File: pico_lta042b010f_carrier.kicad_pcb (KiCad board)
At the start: 2 copper layers, 100 x 52 mm, 31 parts, among them J1 LTA042B010F_FFC_36P_0.5mm, J2 USB-C 5V INPUT, J3 CCFL_INVERTER_13V8, U1 RaspberryPi_Pico_2W, U3 MC34063AD

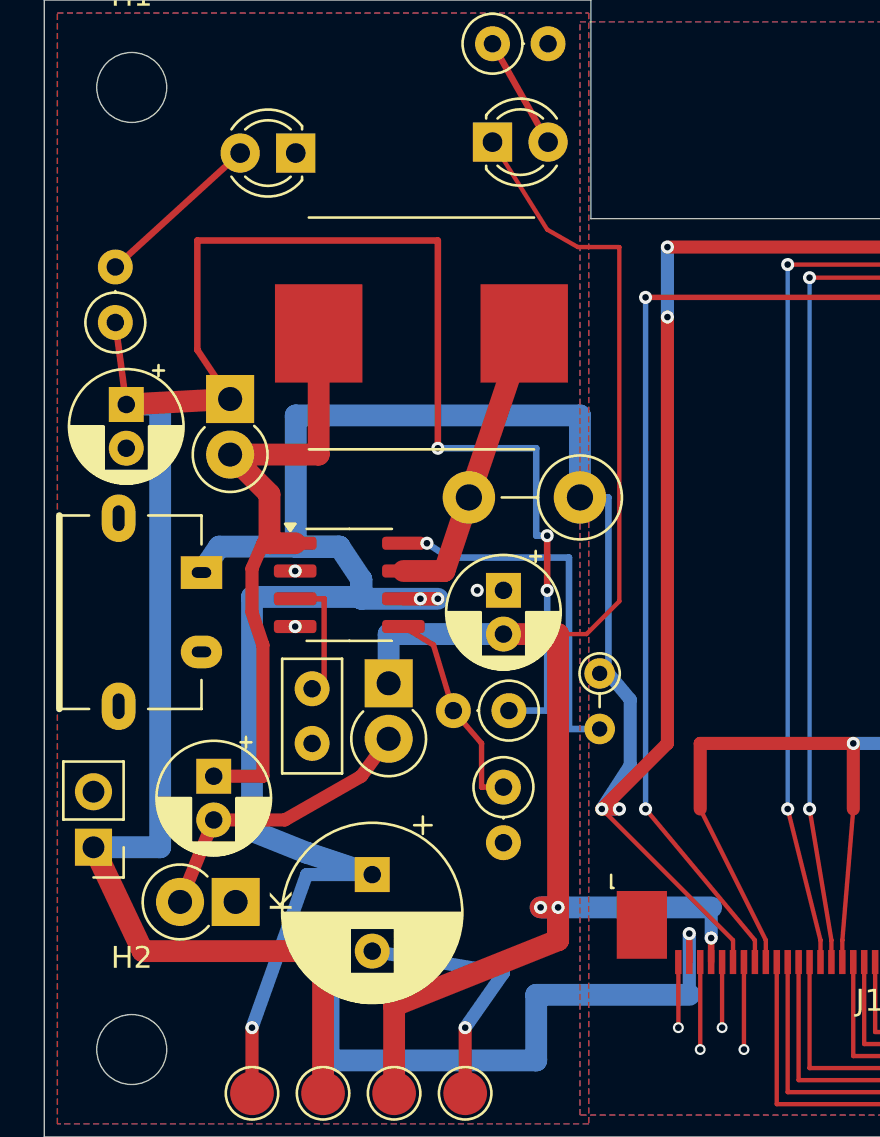
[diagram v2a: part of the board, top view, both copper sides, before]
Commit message: Widen 13V rails across PCB
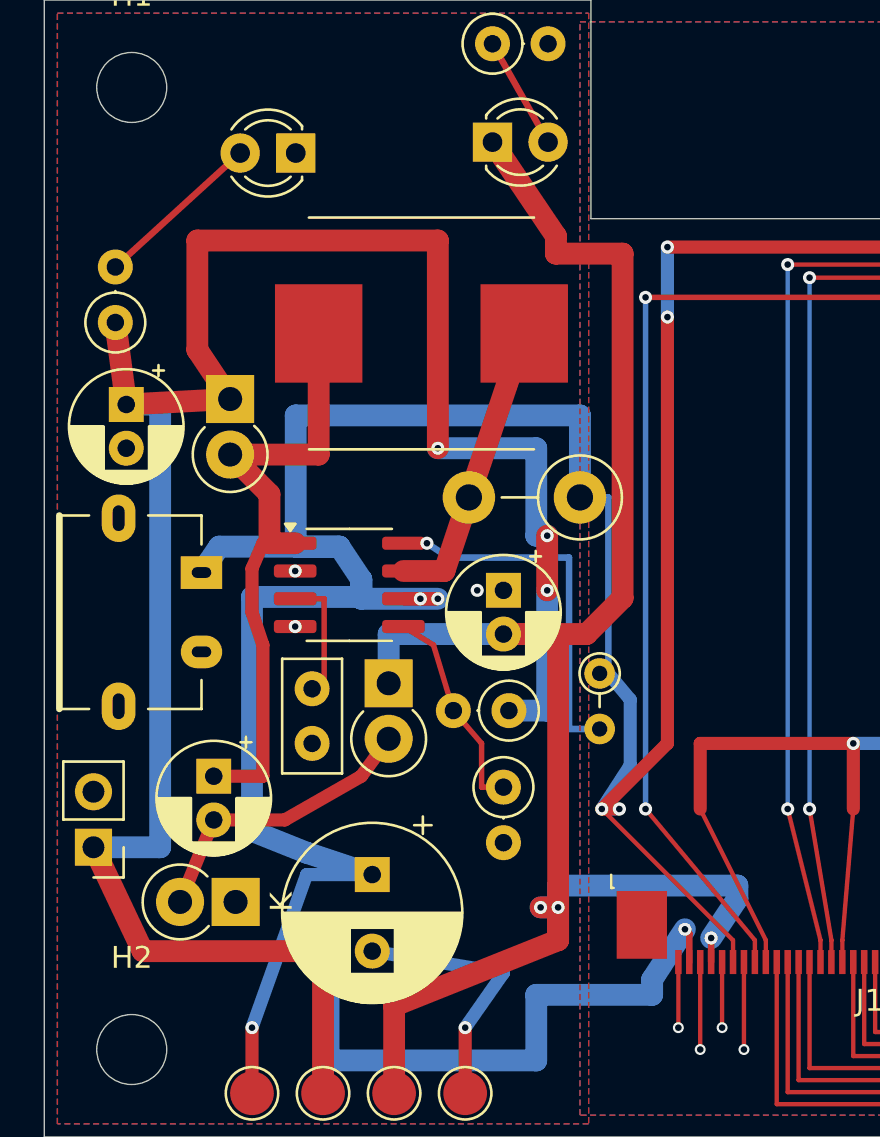
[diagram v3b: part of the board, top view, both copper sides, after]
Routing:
- net -13V8: track 79.0 -> 83.2 mm
- net +13V8: track 132.2 -> 131.4 mm
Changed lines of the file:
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@@
 			(pinfunction "+")
 			(pintype "passive")
+			(thermal_bridge_angle 45)
 		)
 		(pad "2" thru_hole circle
@@
 	)
 	(segment
+		(start 29.5 44)
+		(end 29.5 42.7)
+		(width 0.3)
+		(layer "F.Cu")
+		(net 3)
+	)
+	(segment
 		(start 4.5 43.5)
 		(end 12.75 43.5)
@@
 		(start 7 11)
 		(end 18 11)
-		(width 0.3)
+		(width 1)
 		(layer "F.Cu")
 		(net 3)
@@
 	)
 	(segment
+		(start 29.5 42.7)
+		(end 29.3 42.5)
+		(width 0.3)
+		(layer "F.Cu")
+		(net 3)
+	)
+	(segment
 		(start 3.75 18.5)
 		(end 3.25 14.75)
-		(width 0.3)
+		(width 1)
 		(layer "F.Cu")
 		(net 3)
@@
 		(start 23 24.5)
 		(end 23 27)
-		(width 0.3)
+		(width 1)
 		(layer "F.Cu")
 		(net 3)
@@
 	)
 	(segment
-		(start 29.5 44)
-		(end 29.5 42.7)
-		(width 0.3)
-		(layer "F.Cu")
-		(net 3)
-	)
-	(segment
 		(start 7 16)
 		(end 7 11)
-		(width 0.3)
+		(width 1)
 		(layer "F.Cu")
 		(net 3)
@@
 		(start 18 11)
 		(end 18 20.5)
-		(width 0.3)
+		(width 1)
 		(layer "F.Cu")
 		(net 3)
@@
 		(start 8.5 18.25)
 		(end 7 16)
-		(width 0.3)
+		(width 1)
 		(layer "F.Cu")
 		(net 3)
@@
 	)
 	(via
-		(at 23 24.5)
+		(at 29.3 42.5)
 		(size 0.6)
 		(drill 0.3)
@@
 	)
 	(via
-		(at 23 27)
+		(at 23 24.5)
 		(size 0.6)
 		(drill 0.3)
@@
 	)
 	(via
-		(at 29.5 42.7)
+		(at 23 27)
 		(size 0.6)
 		(drill 0.3)
@@
 	)
 	(segment
-		(start 29.5 42.7)
-		(end 29.5 45.5)
-		(width 0.6)
-		(layer "B.Cu")
-		(net 3)
-	)
-	(segment
 		(start 18 20.5)
 		(end 22.5 20.5)
-		(width 0.3)
+		(width 1)
 		(layer "B.Cu")
 		(net 3)
@@
 		(start 22.5 24.5)
 		(end 23 24.5)
-		(width 0.3)
+		(width 1)
 		(layer "B.Cu")
 		(net 3)
@@
 	)
 	(segment
-		(start 29.5 45.5)
-		(end 22.5 45.5)
-		(width 1)
-		(layer "B.Cu")
-		(net 3)
-	)
-	(segment
 		(start 13 42.7)
 		(end 12.2 42.7)
@@
 		(start 23 27)
 		(end 23 32.5)
-		(width 0.3)
+		(width 1)
 		(layer "B.Cu")
 		(net 3)
@@
 	)
 	(segment
+		(start 27.8 44.8)
+		(end 27.8 45.5)
+		(width 1)
+		(layer "B.Cu")
+		(net 3)
+	)
+	(segment
 		(start 22.5 45.5)
 		(end 22.5 48.5)
@@
 	)
 	(segment
+		(start 29.3 42.5)
+		(end 27.8 44.8)
+		(width 1)
+		(layer "B.Cu")
+		(net 3)
+	)
+	(segment
 		(start 23 32.5)
 		(end 21.25 32.5)
-		(width 0.3)
+		(width 1)
+		(layer "B.Cu")
+		(net 3)
+	)
+	(segment
+		(start 27.8 45.5)
+		(end 22.5 45.5)
+		(width 1)
 		(layer "B.Cu")
 		(net 3)
@@
 		(start 22.5 20.5)
 		(end 22.5 24.5)
-		(width 0.3)
+		(width 1)
 		(layer "B.Cu")
 		(net 3)
@@
 	)
 	(segment
-		(start 24.4 11.3)
-		(end 23 10.5)
-		(width 0.2)
+		(start 24.8 29)
+		(end 26.45 27.35)
+		(width 1)
 		(layer "F.Cu")
 		(net 4)
@@
 	)
 	(segment
-		(start 23.5 29)
-		(end 23.5 43)
+		(start 23.4 11.6)
+		(end 23.4 10.8)
 		(width 1)
 		(layer "F.Cu")
@@
 	)
 	(segment
-		(start 21 29)
-		(end 23.5 29)
+		(start 23.5 29)
+		(end 23.5 43)
 		(width 1)
 		(layer "F.Cu")
@@
 	(segment
 		(start 21 29)
-		(end 24.8 29)
-		(width 0.2)
+		(end 23.5 29)
+		(width 1)
 		(layer "F.Cu")
 		(net 4)
@@
 	)
 	(segment
-		(start 23 10.5)
-		(end 20.5 6.5)
-		(width 0.2)
+		(start 21 29)
+		(end 24.8 29)
+		(width 1)
 		(layer "F.Cu")
 		(net 4)
 	)
 	(segment
-		(start 26.3 11.3)
-		(end 24.4 11.3)
-		(width 0.2)
+		(start 23.4 10.8)
+		(end 20.5 6.5)
+		(width 1)
 		(layer "F.Cu")
 		(net 4)
 	)
 	(segment
-		(start 24.8 29)
-		(end 26.3 27.5)
-		(width 0.2)
+		(start 26.45 27.35)
+		(end 26.45 11.6)
+		(width 1)
 		(layer "F.Cu")
 		(net 4)
 	)
 	(segment
-		(start 23.5 41.5)
-		(end 23.5 43)
+		(start 26.45 11.6)
+		(end 23.4 11.6)
 		(width 1)
 		(layer "F.Cu")
@@
 	)
 	(segment
-		(start 26.3 27.5)
-		(end 26.3 11.3)
-		(width 0.2)
+		(start 23.5 41.5)
+		(end 23.5 43)
+		(width 1)
 		(layer "F.Cu")
 		(net 4)
@@
 	)
 	(segment
+		(start 31.7 41.1)
+		(end 31.7 40.5)
+		(width 1)
+		(layer "B.Cu")
+		(net 4)
+	)
+	(segment
 		(start 15.75 31.25)
 		(end 15.75 29)
@@
 	)
 	(segment
-		(start 15.75 29)
-		(end 21 29)
+		(start 23.5 40.5)
+		(end 23.5 41.5)
+		(width 1)
+		(layer "B.Cu")
+		(net 4)
+	)
+	(segment
+		(start 31.7 40.5)
+		(end 23.5 40.5)
 		(width 1)
 		(layer "B.Cu")
@@
 	(segment
 		(start 30.5 42.9)
-		(end 30.5 41.5)
-		(width 0.6)
+		(end 31.7 41.1)
+		(width 1)
 		(layer "B.Cu")
 		(net 4)
 	)
 	(segment
-		(start 30.5 41.5)
-		(end 23.5 41.5)
+		(start 15.75 29)
+		(end 21 29)
 		(width 1)
 		(layer "B.Cu")

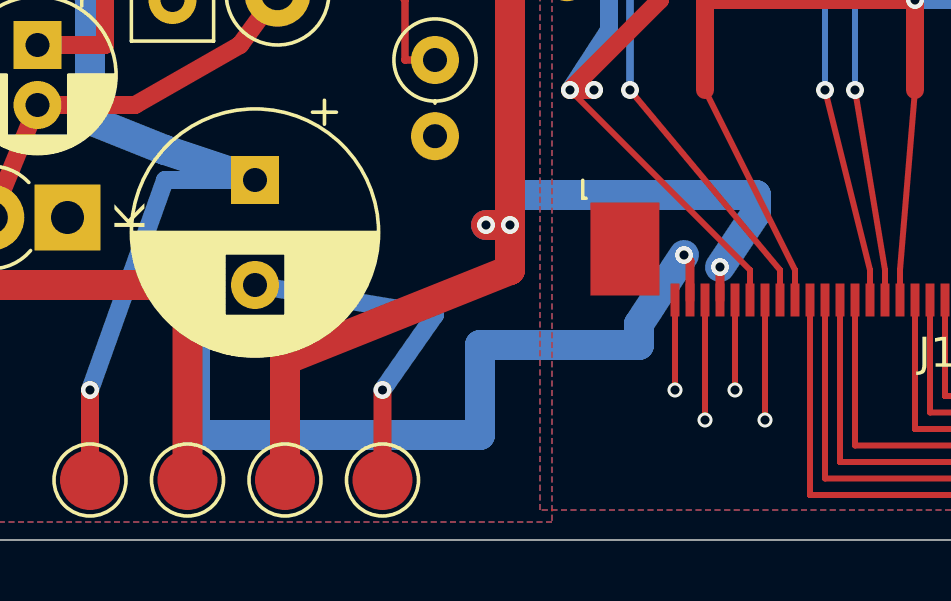
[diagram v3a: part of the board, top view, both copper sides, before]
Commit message: Optimize J1 bias rail routing
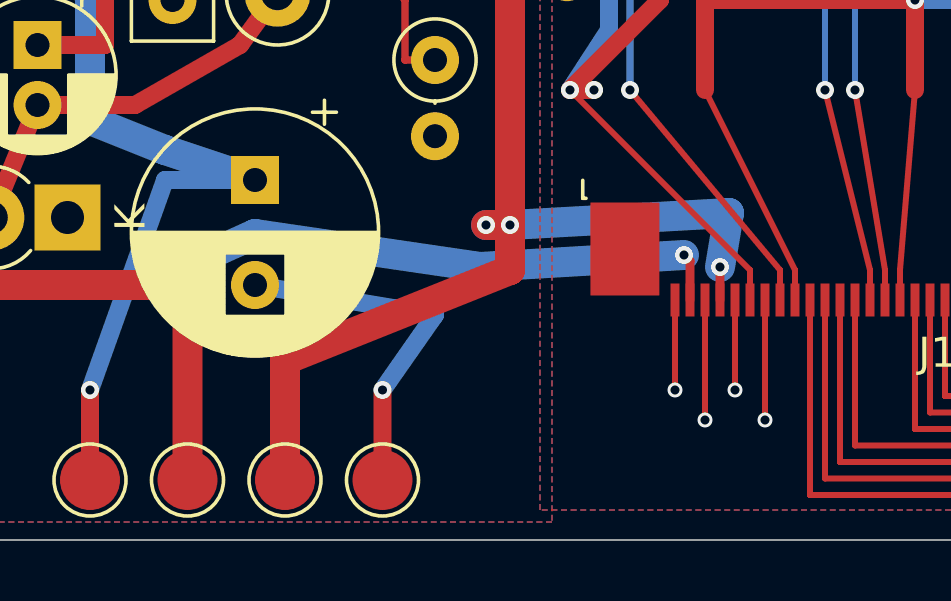
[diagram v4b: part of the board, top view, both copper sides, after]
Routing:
- net +13V8: track 131.4 -> 121.0 mm
- net -13V8: track 83.2 -> 80.3 mm
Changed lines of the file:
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@@
-	)
-	(segment
-		(start 13 48.5)
-		(end 13 42.7)
-		(width 1)
-		(layer "B.Cu")
-		(net 3)
 	)
 	(segment
@@
 	)
 	(segment
-		(start 27.8 44.8)
-		(end 27.8 45.5)
-		(width 1)
-		(layer "B.Cu")
-		(net 3)
-	)
-	(segment
-		(start 22.5 45.5)
-		(end 22.5 48.5)
-		(width 1)
-		(layer "B.Cu")
-		(net 3)
-	)
-	(segment
 		(start 29.3 42.5)
-		(end 27.8 44.8)
+		(end 22.5 42.9)
+		(width 1)
+		(layer "B.Cu")
+		(net 3)
+	)
+	(segment
+		(start 22.5 42.9)
+		(end 15 41.8)
 		(width 1)
 		(layer "B.Cu")
@@
 	)
 	(segment
-		(start 27.8 45.5)
-		(end 22.5 45.5)
+		(start 15 41.8)
+		(end 13 42.7)
 		(width 1)
 		(layer "B.Cu")
@@
 		(start 5.3 18.5)
 		(end 5.3 38.75)
-		(width 1)
-		(layer "B.Cu")
-		(net 3)
-	)
-	(segment
-		(start 22.5 48.5)
-		(end 13 48.5)
 		(width 1)
 		(layer "B.Cu")
@@
 	)
 	(segment
-		(start 31.7 41.1)
-		(end 31.7 40.5)
-		(width 1)
-		(layer "B.Cu")
-		(net 4)
-	)
-	(segment
 		(start 15.75 31.25)
 		(end 15.75 29)
@@
 	)
 	(segment
-		(start 23.5 40.5)
+		(start 30.8 41.1)
 		(end 23.5 41.5)
-		(width 1)
-		(layer "B.Cu")
-		(net 4)
-	)
-	(segment
-		(start 31.7 40.5)
-		(end 23.5 40.5)
-		(width 1)
-		(layer "B.Cu")
-		(net 4)
-	)
-	(segment
-		(start 30.5 42.9)
-		(end 31.7 41.1)
 		(width 1)
 		(layer "B.Cu")
@@
 		(width 1)
 		(layer "B.Cu")
+		(net 4)
+	)
+	(segment
+		(start 30.5 42.9)
+		(end 30.8 41.1)
+		(width 1)
+		(layer "B.Cu")

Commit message: Clean up silkscreen and add board ID
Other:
- board text added: "PICO2W-LTA042B010F"
- board text added: "REV A 2026-09-17"
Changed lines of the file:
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@@
 		(tags "mounting hole 3.2mm no annular m3")
 		(property "Reference" "H1"
-			(at 0 -4.2 0)
+			(at 0 4 0)
 			(layer "F.SilkS")
 			(effects
@@
 		(tags "mounting hole 3.2mm no annular m3")
 		(property "Reference" "H4"
-			(at 0 -4.2 0)
+			(at 0 4 0)
 			(layer "F.SilkS")
 			(effects
@@
 		)
 		(fp_text user "K"
-			(at -2.1 0 90)
+			(at -2.1 2.25 90)
 			(layer "F.SilkS")
 			(effects
@@
 		(layer "Edge.Cuts")
 	)
+	(gr_text "REV A  2026-09-17"
+		(at 37.5 16 0)
+		(layer "F.SilkS")
+		(effects
+			(font
+				(size 1 1)
+				(thickness 0.15)
+			)
+		)
+	)
+	(gr_text "PICO2W-LTA042B010F"
+		(at 37.5 14 0)
+		(layer "F.SilkS")
+		(effects
+			(font
+				(size 1.2 1.2)
+				(thickness 0.18)
+			)
+		)
+	)
 	(gr_text "NO COPPER ROUTING YET"
